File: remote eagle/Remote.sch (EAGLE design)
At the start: 17 parts, among them IC1 ATmega328p, J1 ISP Touch, Y1 16MHz, Y2 ANTENNA2SMD5

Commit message: Revision 12 of the board, complete with RFM22B RF module.
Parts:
- Y2: value ANTENNA2SMD5 -> ANTENNA2ANTENNA-CHIP_1204; device SparkFun:ANTENNA2SMD5 -> remote:ANTENNA2ANTENNA-CHIP_1204
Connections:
- net SHUTDOWN: now also IC1.PD3(INT1)
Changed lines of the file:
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@@
 <grid distance="0.1" unitdist="inch" unit="inch" style="lines" multiple="1" display="no" altdistance="0.01" altunitdist="inch" altunit="inch"/>
 <layers>
-<layer number="1" name="Top" color="4" fill="1" visible="yes" active="no"/>
-<layer number="2" name="Route2" color="1" fill="3" visible="yes" active="no"/>
-<layer number="3" name="Route3" color="4" fill="3" visible="yes" active="no"/>
-<layer number="4" name="Route4" color="1" fill="4" visible="yes" active="no"/>
-<layer number="5" name="Route5" color="4" fill="4" visible="yes" active="no"/>
-<layer number="6" name="Route6" color="1" fill="8" visible="yes" active="no"/>
-<layer number="7" name="Route7" color="4" fill="8" visible="yes" active="no"/>
-<layer number="8" name="Route8" color="1" fill="2" visible="yes" active="no"/>
-<layer number="9" name="Route9" color="4" fill="2" visible="yes" active="no"/>
-<layer number="10" name="Route10" color="1" fill="7" visible="yes" active="no"/>
-<layer number="11" name="Route11" color="4" fill="7" visible="yes" active="no"/>
-<layer number="12" name="Route12" color="1" fill="5" visible="yes" active="no"/>
-<layer number="13" name="Route13" color="4" fill="5" visible="yes" active="no"/>
-<layer number="14" name="Route14" color="1" fill="6" visible="yes" active="no"/>
-<layer number="15" name="Route15" color="4" fill="6" visible="yes" active="no"/>
-<layer number="16" name="Bottom" color="1" fill="1" visible="yes" active="no"/>
-<layer number="17" name="Pads" color="2" fill="1" visible="yes" active="no"/>
-<layer number="18" name="Vias" color="2" fill="1" visible="yes" active="no"/>
-<layer number="19" name="Unrouted" color="6" fill="1" visible="yes" active="no"/>
-<layer number="20" name="Dimension" color="15" fill="1" visible="yes" active="no"/>
-<layer number="21" name="tPlace" color="7" fill="1" visible="yes" active="no"/>
-<layer number="22" name="bPlace" color="7" fill="1" visible="yes" active="no"/>
-<layer number="23" name="tOrigins" color="15" fill="1" visible="yes" active="no"/>
-<layer number="24" name="bOrigins" color="15" fill="1" visible="yes" active="no"/>
-<layer number="25" name="tNames" color="7" fill="1" visible="yes" active="no"/>
-<layer number="26" name="bNames" color="7" fill="1" visible="yes" active="no"/>
-<layer number="27" name="tValues" color="7" fill="1" visible="yes" active="no"/>
-<layer number="28" name="bValues" color="7" fill="1" visible="yes" active="no"/>
+<layer number="1" name="Top" color="4" fill="1" visible="no" active="no"/>
+<layer number="2" name="Route2" color="1" fill="3" visible="no" active="no"/>
+<layer number="3" name="Route3" color="4" fill="3" visible="no" active="no"/>
+<layer number="4" name="Route4" color="1" fill="4" visible="no" active="no"/>
+<layer number="5" name="Route5" color="4" fill="4" visible="no" active="no"/>
+<layer number="6" name="Route6" color="1" fill="8" visible="no" active="no"/>
+<layer number="7" name="Route7" color="4" fill="8" visible="no" active="no"/>
+<layer number="8" name="Route8" color="1" fill="2" visible="no" active="no"/>
+<layer number="9" name="Route9" color="4" fill="2" visible="no" active="no"/>
+<layer number="10" name="Route10" color="1" fill="7" visible="no" active="no"/>
+<layer number="11" name="Route11" color="4" fill="7" visible="no" active="no"/>
+<layer number="12" name="Route12" color="1" fill="5" visible="no" active="no"/>
+<layer number="13" name="Route13" color="4" fill="5" visible="no" active="no"/>
+<layer number="14" name="Route14" color="1" fill="6" visible="no" active="no"/>
+<layer number="15" name="Route15" color="4" fill="6" visible="no" active="no"/>
+<layer number="16" name="Bottom" color="1" fill="1" visible="no" active="no"/>
+<layer number="17" name="Pads" color="2" fill="1" visible="no" active="no"/>
+<layer number="18" name="Vias" color="2" fill="1" visible="no" active="no"/>
+<layer number="19" name="Unrouted" color="6" fill="1" visible="no" active="no"/>
+<layer number="20" name="Dimension" color="15" fill="1" visible="no" active="no"/>
+<layer number="21" name="tPlace" color="7" fill="1" visible="no" active="no"/>
+<layer number="22" name="bPlace" color="7" fill="1" visible="no" active="no"/>
+<layer number="23" name="tOrigins" color="15" fill="1" visible="no" active="no"/>
+<layer number="24" name="bOrigins" color="15" fill="1" visible="no" active="no"/>
+<layer number="25" name="tNames" color="7" fill="1" visible="no" active="no"/>
+<layer number="26" name="bNames" color="7" fill="1" visible="no" active="no"/>
+<layer number="27" name="tValues" color="7" fill="1" visible="no" active="no"/>
+<layer number="28" name="bValues" color="7" fill="1" visible="no" active="no"/>
 <layer number="29" name="tStop" color="7" fill="3" visible="no" active="no"/>
 <layer number="30" name="bStop" color="7" fill="6" visible="no" active="no"/>
@@
 <layer number="35" name="tGlue" color="7" fill="4" visible="no" active="no"/>
 <layer number="36" name="bGlue" color="7" fill="5" visible="no" active="no"/>
-<layer number="37" name="tTest" color="7" fill="1" visible="yes" active="no"/>
-<layer number="38" name="bTest" color="7" fill="1" visible="yes" active="no"/>
+<layer number="37" name="tTest" color="7" fill="1" visible="no" active="no"/>
+<layer number="38" name="bTest" color="7" fill="1" visible="no" active="no"/>
 <layer number="39" name="tKeepout" color="4" fill="11" visible="no" active="no"/>
 <layer number="40" name="bKeepout" color="1" fill="11" visible="no" active="no"/>
@@
 <layer number="44" name="Drills" color="7" fill="1" visible="no" active="no"/>
 <layer number="45" name="Holes" color="7" fill="1" visible="no" active="no"/>
-<layer number="46" name="Milling" color="3" fill="1" visible="yes" active="no"/>
-<layer number="47" name="Measures" color="7" fill="1" visible="yes" active="no"/>
-<layer number="48" name="Document" color="7" fill="1" visible="yes" active="no"/>
-<layer number="49" name="Reference" color="7" fill="1" visible="yes" active="no"/>
-<layer number="50" name="dxf" color="7" fill="1" visible="yes" active="no"/>
-<layer number="51" name="tDocu" color="7" fill="1" visible="yes" active="no"/>
-<layer number="52" name="bDocu" color="7" fill="1" visible="yes" active="no"/>
-<layer number="53" name="tGND_GNDA" color="7" fill="9" visible="yes" active="no"/>
-<layer number="54" name="bGND_GNDA" color="1" fill="9" visible="yes" active="no"/>
-<layer number="56" name="wert" color="7" fill="1" visible="yes" active="no"/>
-<layer number="57" name="tCAD" color="7" fill="1" visible="yes" active="no"/>
+<layer number="46" name="Milling" color="3" fill="1" visible="no" active="no"/>
+<layer number="47" name="Measures" color="7" fill="1" visible="no" active="no"/>
+<layer number="48" name="Document" color="7" fill="1" visible="no" active="no"/>
+<layer number="49" name="Reference" color="7" fill="1" visible="no" active="no"/>
+<layer number="50" name="dxf" color="7" fill="1" visible="no" active="no"/>
+<layer number="51" name="tDocu" color="7" fill="1" visible="no" active="no"/>
+<layer number="52" name="bDocu" color="7" fill="1" visible="no" active="no"/>
+<layer number="53" name="tGND_GNDA" color="7" fill="9" visible="no" active="no"/>
+<layer number="54" name="bGND_GNDA" color="1" fill="9" visible="no" active="no"/>
+<layer number="56" name="wert" color="7" fill="1" visible="no" active="no"/>
+<layer number="57" name="tCAD" color="7" fill="1" visible="no" active="no"/>
 <layer number="91" name="Nets" color="2" fill="1" visible="yes" active="yes"/>
 <layer number="92" name="Busses" color="1" fill="1" visible="yes" active="yes"/>
@@
 <part name="P+2" library="supply1" deviceset="VCC" device=""/>
 <part name="GND8" library="SparkFun" deviceset="GND" device=""/>
-<part name="Y2" library="SparkFun" deviceset="ANTENNA2" device="SMD5"/>
+<part name="Y2" library="remote" deviceset="ANTENNA2" device="ANTENNA-CHIP_1204"/>
 <part name="LOGO" library="remote" deviceset="TURNTOUCHLOGO" device="200DPI"/>
 <part name="U$6" library="remote" deviceset="COINCELLHOLDER" device=""/>
@@
 <pinref part="U$5" gate="G$1" pin="SDN"/>
 </segment>
-</net>
+<segment>
+<pinref part="IC1" gate="G$1" pin="PD3(INT1)"/>
+<wire x1="68.58" y1="40.64" x2="71.12" y2="40.64" width="0.1524" layer="91"/>
+<label x="71.12" y="40.64" size="1.016" layer="95" xref="yes"/>
+</segment>
+</net>

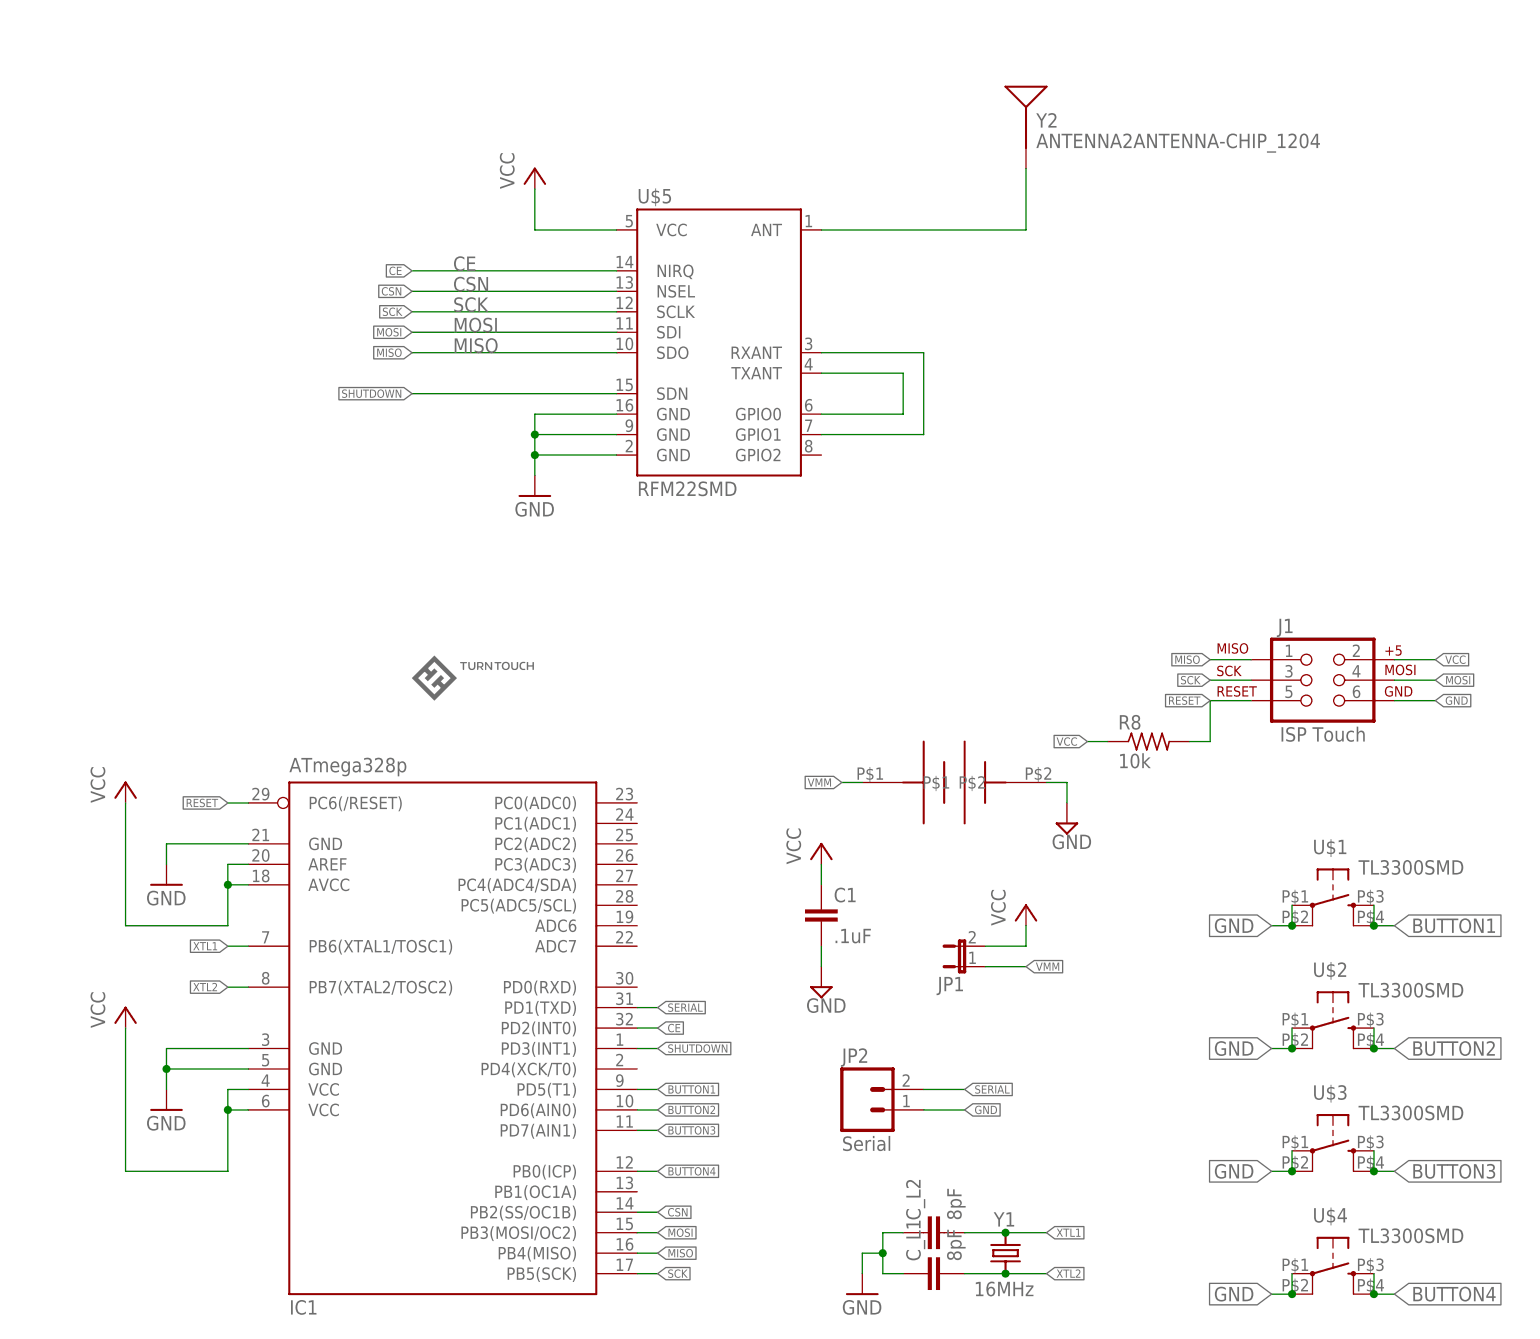
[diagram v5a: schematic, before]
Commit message: Revision 13, with new snaptron dome buttons.
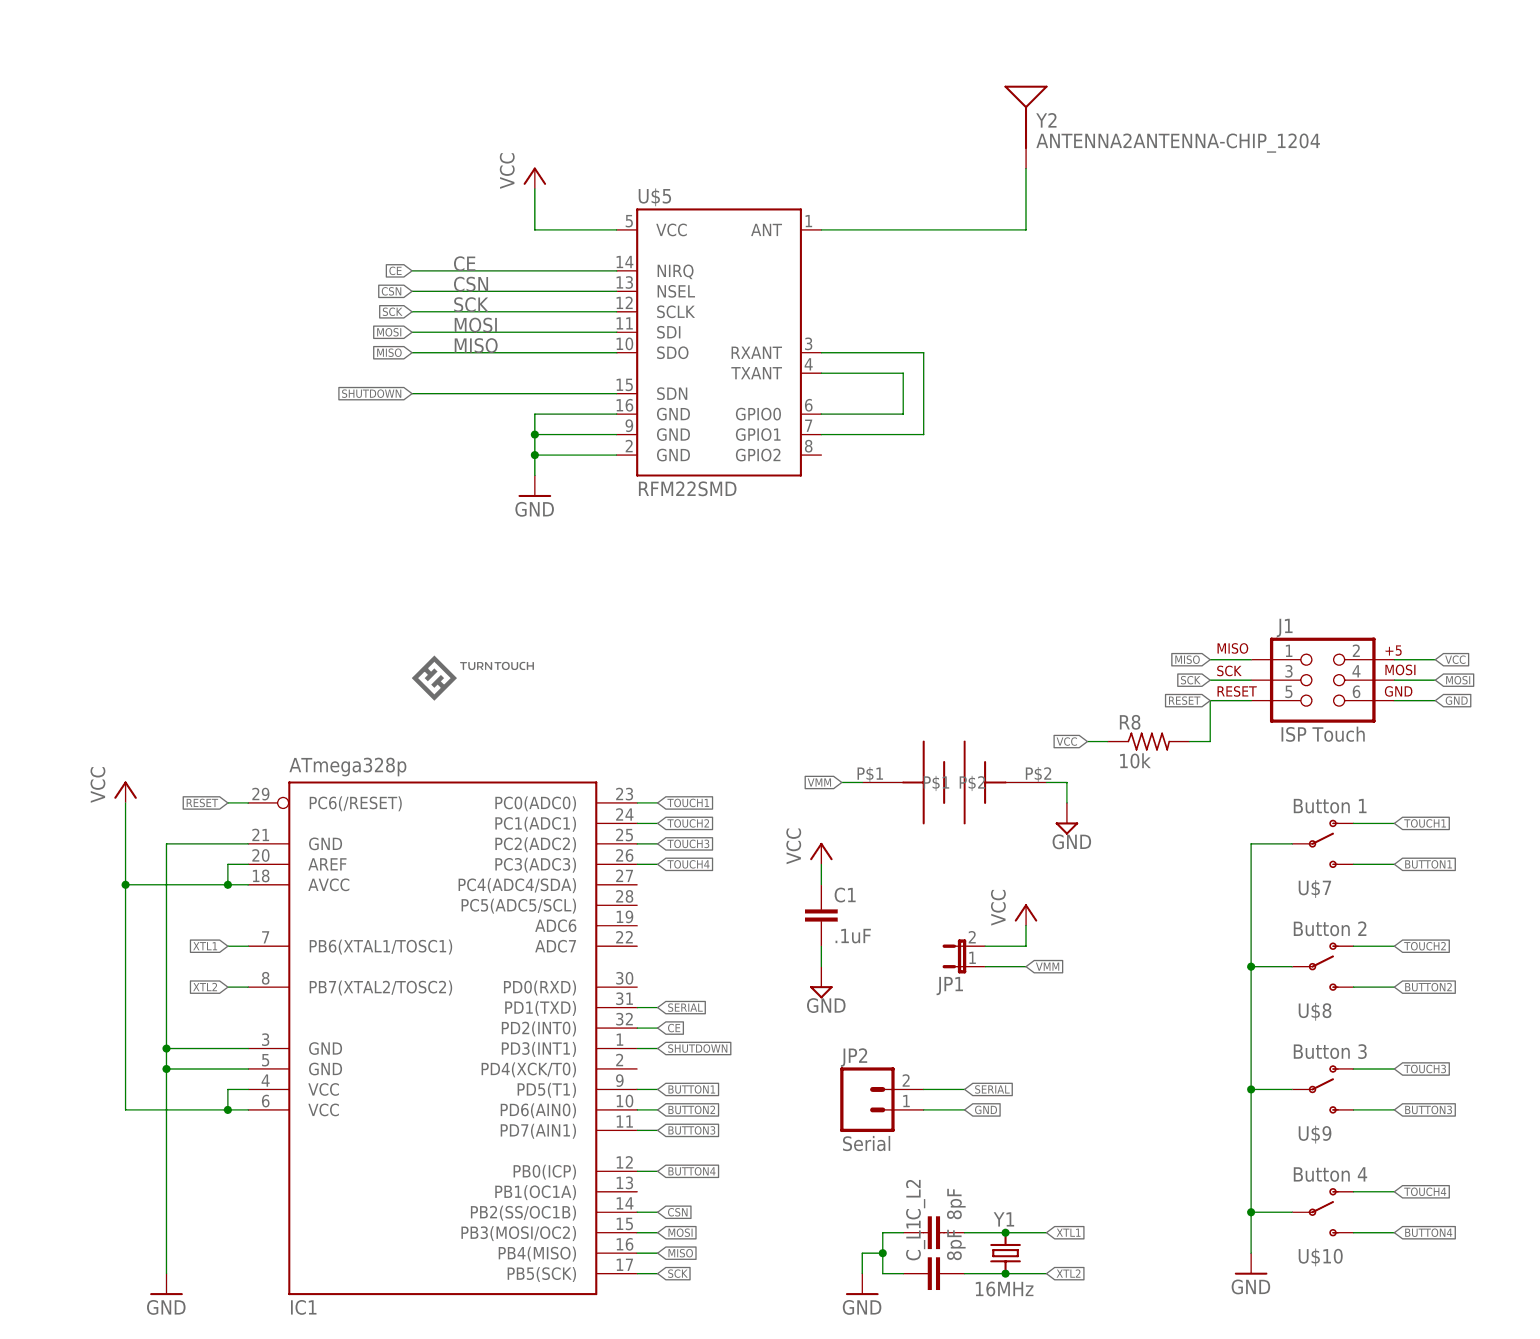
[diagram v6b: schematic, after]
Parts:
- removed U$1, U$2, U$3, U$4: TL3300SMD, remote:TL3300SMD
- added U$10: Button 4, remote:SWITCH-SPDT-SMDSMD2
- added U$7: Button 1, remote:SWITCH-SPDT-SMDSMD2
- added U$8: Button 2, remote:SWITCH-SPDT-SMDSMD2
- added U$9: Button 3, remote:SWITCH-SPDT-SMDSMD2
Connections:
- new net TOUCH1: IC1.PC0(ADC0), U$7.TOUCH
- new net TOUCH2: IC1.PC1(ADC1), U$8.TOUCH
- new net TOUCH3: IC1.PC2(ADC2), U$9.TOUCH
- new net TOUCH4: IC1.PC3(ADC3), U$10.TOUCH
- net BUTTON1: now also U$7.BUTTON; no longer U$1.S, U$1.S1
- net BUTTON2: now also U$8.BUTTON; no longer U$2.S, U$2.S1
- net BUTTON3: now also U$9.BUTTON; no longer U$3.S, U$3.S1
- net BUTTON4: now also U$10.BUTTON; no longer U$4.S, U$4.S1
- net GND: now also U$10.GND, U$7.GND, U$8.GND, U$9.GND; no longer U$1.P, U$1.P1, U$2.P, U$2.P1, U$3.P, U$3.P1, U$4.P, U$4.P1
